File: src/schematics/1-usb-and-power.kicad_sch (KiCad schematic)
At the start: 0 parts

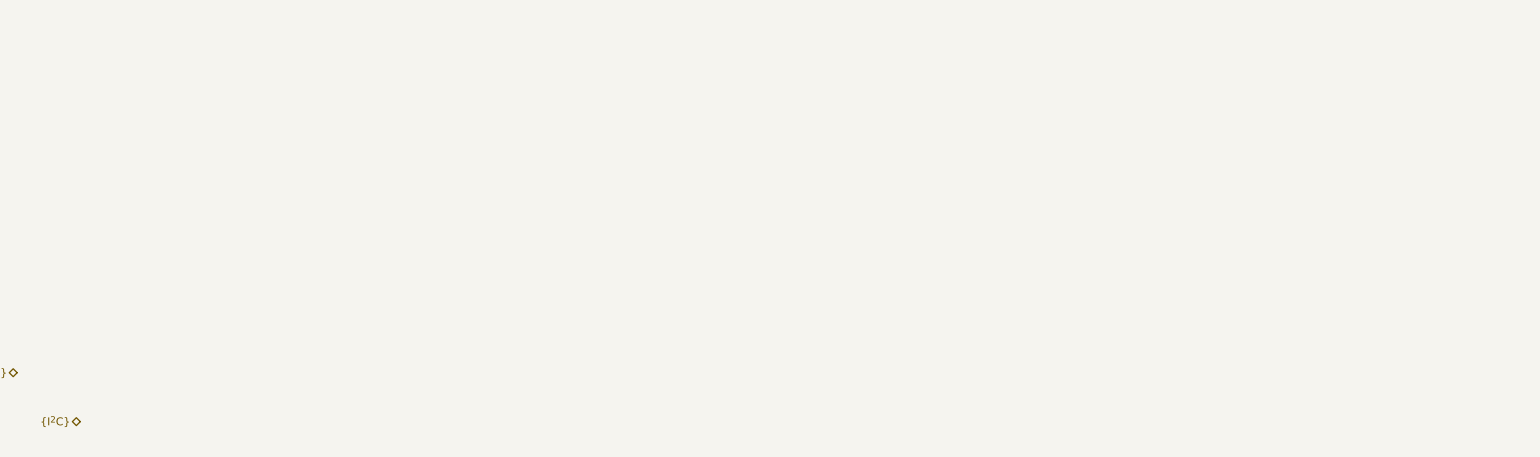
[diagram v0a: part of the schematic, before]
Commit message: Further MCU elaboration and pin mapping.
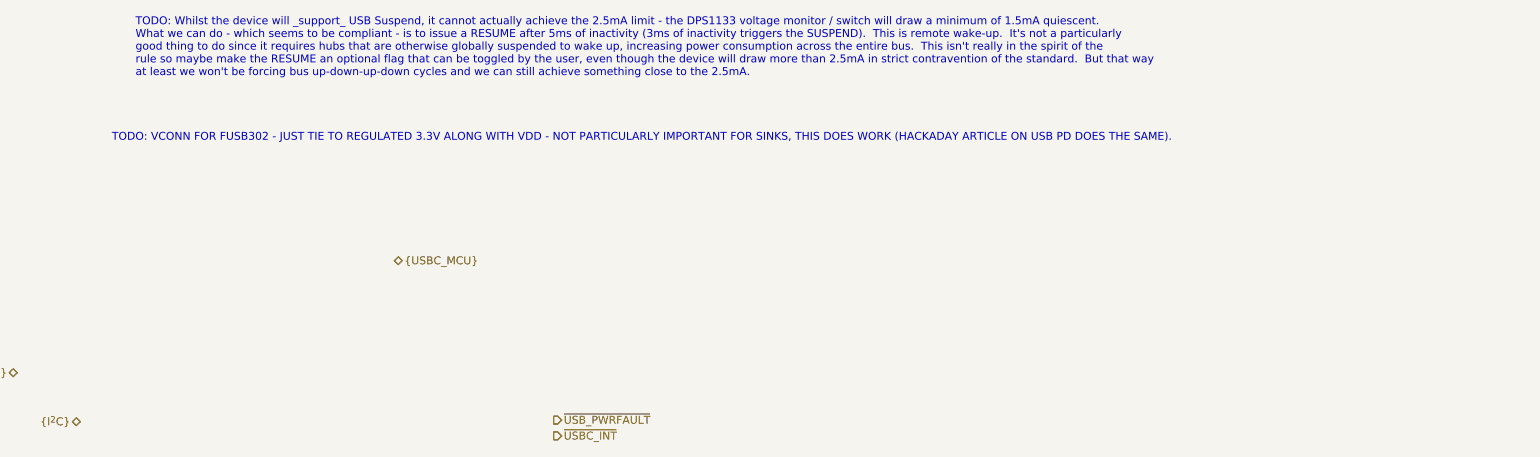
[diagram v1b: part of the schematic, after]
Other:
- note added: "TODO: VCONN FOR FUSB302 - JUST TIE TO REGULATED 3.3V ALONG WITH VDD - NOT PARTICULARLY IMPORTANT FOR SINKS, THIS DOES WORK (HACKADAY ARTICLE ON USB PD DOES THE SAME)."
- note added: "TODO: Whilst the device will _support_ USB Suspend, it cannot actually achieve the 2.5mA limit - the DPS1133 voltage monitor / switch will draw a minimum of 1.5mA quiescent. What we can do - which seems to be compliant - is to issue a RESUME after 5ms of inactivity (3ms of inactivity triggers the SUSPEND). This is remote wake-up. It's not a particularly good thing to do since it requires hubs tha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"
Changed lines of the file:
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@@
     (company "Pete Restall <pete@restall.net>")
+  )
+  (bus_alias "USBC_MCU" (members "D_{+}" "D_{-}"))
+  (text "TODO: VCONN FOR FUSB302 - JUST TIE TO REGULATED 3.3V ALONG WITH VDD - NOT PARTICULARLY IMPORTANT FOR SINKS, THIS DOES WORK (HACKADAY ARTICLE ON USB PD DOES THE SAME)."
+    (at 81.28 82.296 0)
+    (effects (font (size 1.27 1.27)) (justify left bottom))
+  )
+  (text "TODO: Whilst the device will _support_ USB Suspend, it cannot actually achieve the 2.5mA limit - the DPS1133 voltage monitor / switch will draw a minimum of 1.5mA quiescent.\nWhat we can do - which seems to be compliant - is to issue a RESUME after 5ms of inactivity (3ms of inactivity triggers the SUSPEND).  This is remote wake-up.  It's not a particularly\ngood thing to do since it requires hubs that are otherwise globally suspended to wake up, increasing power consumption across the entire bus.  This isn't really in the spirit of the\nrule so maybe make the RESUME an optional flag that can be toggled by the user, even though the device will draw more than 2.5mA in strict contravention of the standard.  But that way\nat least we won't be forcing bus up-down-up-down cycles and we can still achieve something close to the 2.5mA."
+    (at 85.09 71.882 0)
+    (effects (font (size 1.27 1.27)) (justify left bottom))
   )
   (hierarchical_label "{USBC_CONN}" (shape bidirectional) (at 66.04 119.38 180) (fields_autoplaced)
     (effects (font (size 1.27 1.27)) (justify right))
   )
+  (hierarchical_label "~{USBC_INT}" (shape output) (at 152.4 129.54 0) (fields_autoplaced)
+    (effects (font (size 1.27 1.27)) (justify left))
+  )
   (hierarchical_label "USBC_VBUS" (shape input) (at 50.8 101.346 180) (fields_autoplaced)
     (effects (font (size 1.27 1.27)) (justify right))
+  )
+  (hierarchical_label "{USBC_MCU}" (shape bidirectional) (at 126.746 101.346 0) (fields_autoplaced)
+    (effects (font (size 1.27 1.27)) (justify left))
   )
   (hierarchical_label "{I^{2}C}" (shape bidirectional) (at 76.2 127.254 180) (fields_autoplaced)
     (effects (font (size 1.27 1.27)) (justify right))
   )
+  (hierarchical_label "~{USB_PWRFAULT}" (shape output) (at 152.4 127 0) (fields_autoplaced)
+    (effects (font (size 1.27 1.27)) (justify left))
+  )
 )

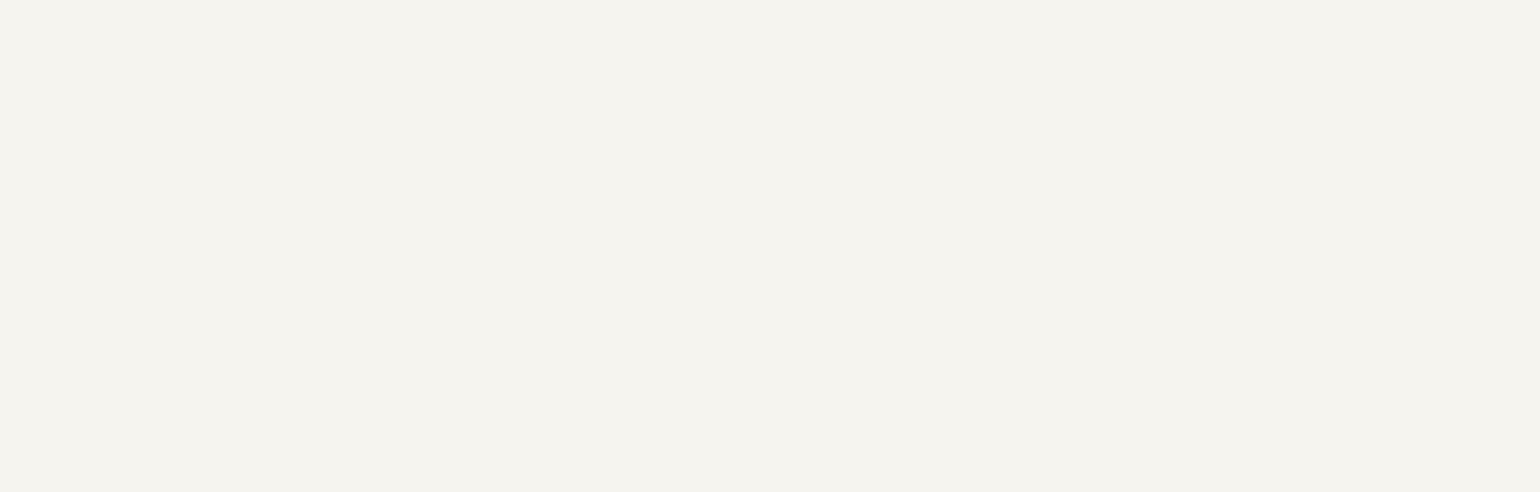
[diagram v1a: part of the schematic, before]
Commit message: Further elaboration of the design, particularly around the power budget.  It's clear that the USB Suspend current of 2.5mA won't be met, mainly due to the DPS1133 power switch's quiescent current.  This is a nice part worth keeping though as it contains OVP, OCP and reverse voltage protection all in one, up to 24V maximum input.
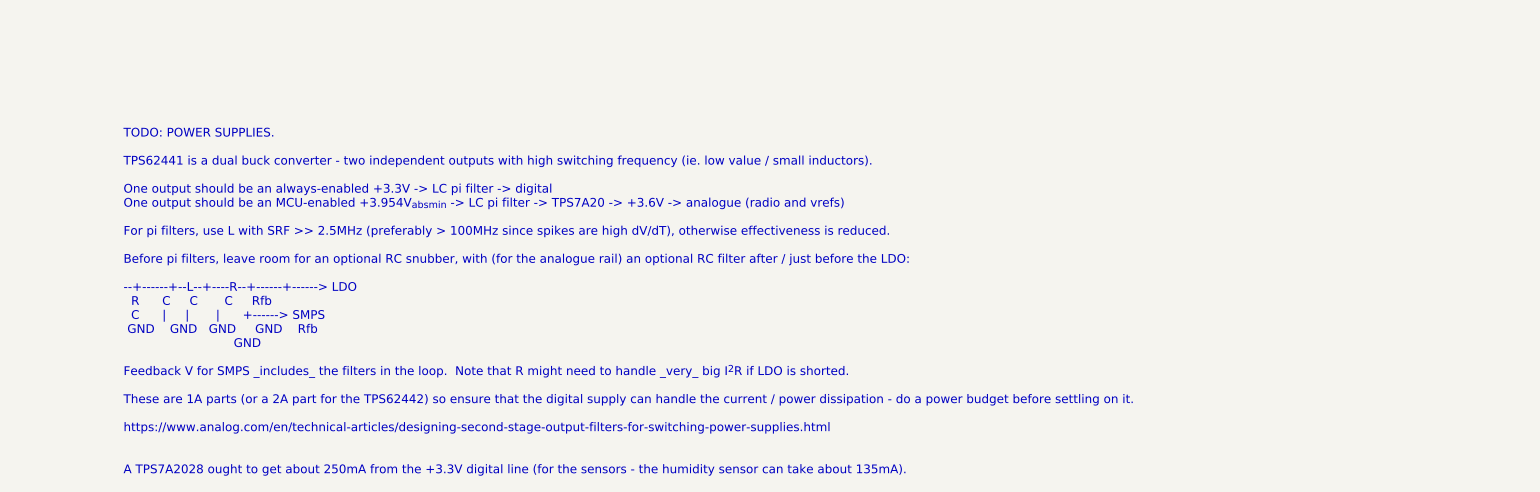
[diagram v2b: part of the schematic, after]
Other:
- note added: "TODO: POWER SUPPLIES. TPS62441 is a dual buck converter - two independent outputs with high switching frequency (ie. low value / small inductors). One output should be an always-enabled +3.3V -> LC pi filter -> digital One output should be an MCU-enabled +3.954V_{absmin} -> LC pi filter -> TPS7A20 -> +3.6V -> analogue (radio and vrefs) For pi filters, use L with SRF >> 2.5MHz (preferably > 100MHz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"
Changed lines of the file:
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@@
+    (effects (font (size 1.27 1.27)) (justify left bottom))
+  )
+  (text "TODO: POWER SUPPLIES.\n\nTPS62441 is a dual buck converter - two independent outputs with high switching frequency (ie. low value / small inductors).\n\nOne output should be an always-enabled +3.3V -> LC pi filter -> digital\nOne output should be an MCU-enabled +3.954V_{absmin} -> LC pi filter -> TPS7A20 -> +3.6V -> analogue (radio and vrefs)\n\nFor pi filters, use L with SRF >> 2.5MHz (preferably > 100MHz since spikes are high dV/dT), otherwise effectiveness is reduced.\n\nBefore pi filters, leave room for an optional RC snubber, with (for the analogue rail) an optional RC filter after / just before the LDO:\n\n--+------+--L--+----R--+------+------> LDO\n  R      C     C       C     Rfb\n  C      |     |       |      +------> SMPS\n GND    GND   GND     GND    Rfb\n                             GND\n\nFeedback V for SMPS _includes_ the filters in the loop.  Note that R might need to handle _very_ big I^{2}R if LDO is shorted.\n\nThese are 1A parts (or a 2A part for the TPS62442) so ensure that the digital supply can handle the current / power dissipation - do a power budget before settling on it.\n\nhttps://www.analog.com/en/technical-articles/designing-second-stage-output-filters-for-switching-power-supplies.html\n\n\nA TPS7A2028 ought to get about 250mA from the +3.3V digital line (for the sensors - the humidity sensor can take about 135mA).\n"
+    (at 138.176 209.804 0)
     (effects (font (size 1.27 1.27)) (justify left bottom))
   )

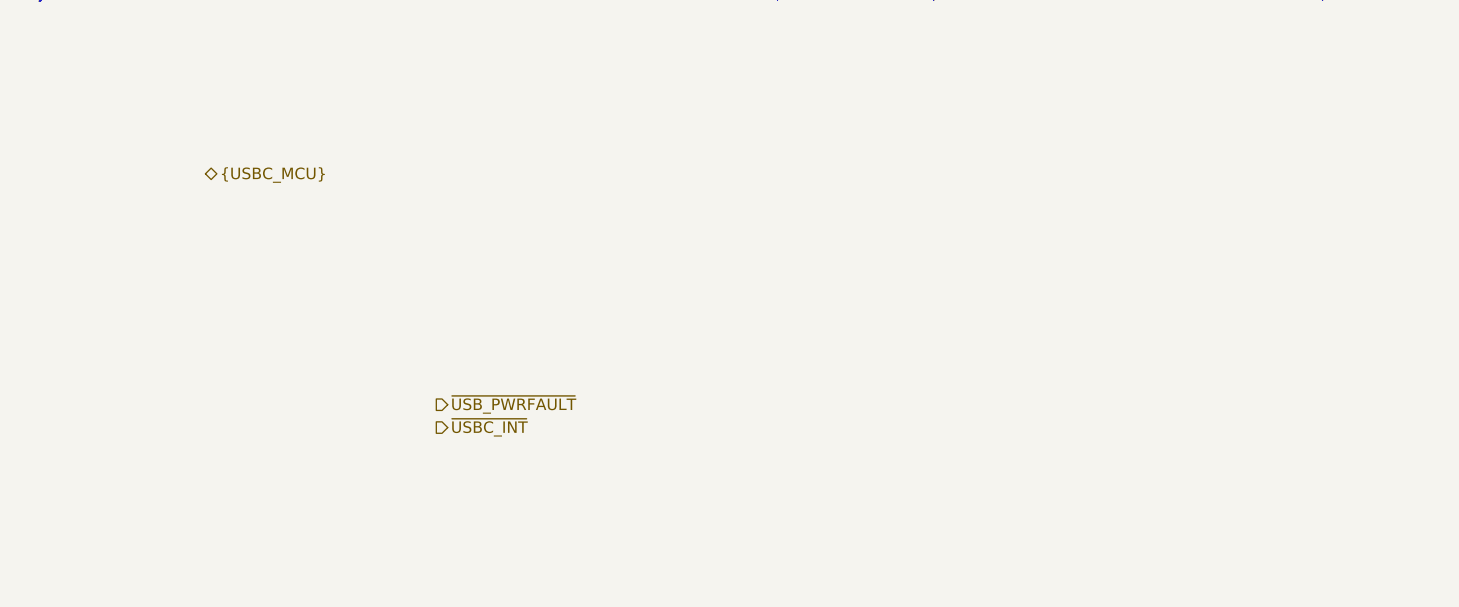
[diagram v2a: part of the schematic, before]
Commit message: Elaboration of the top-level schematicd.
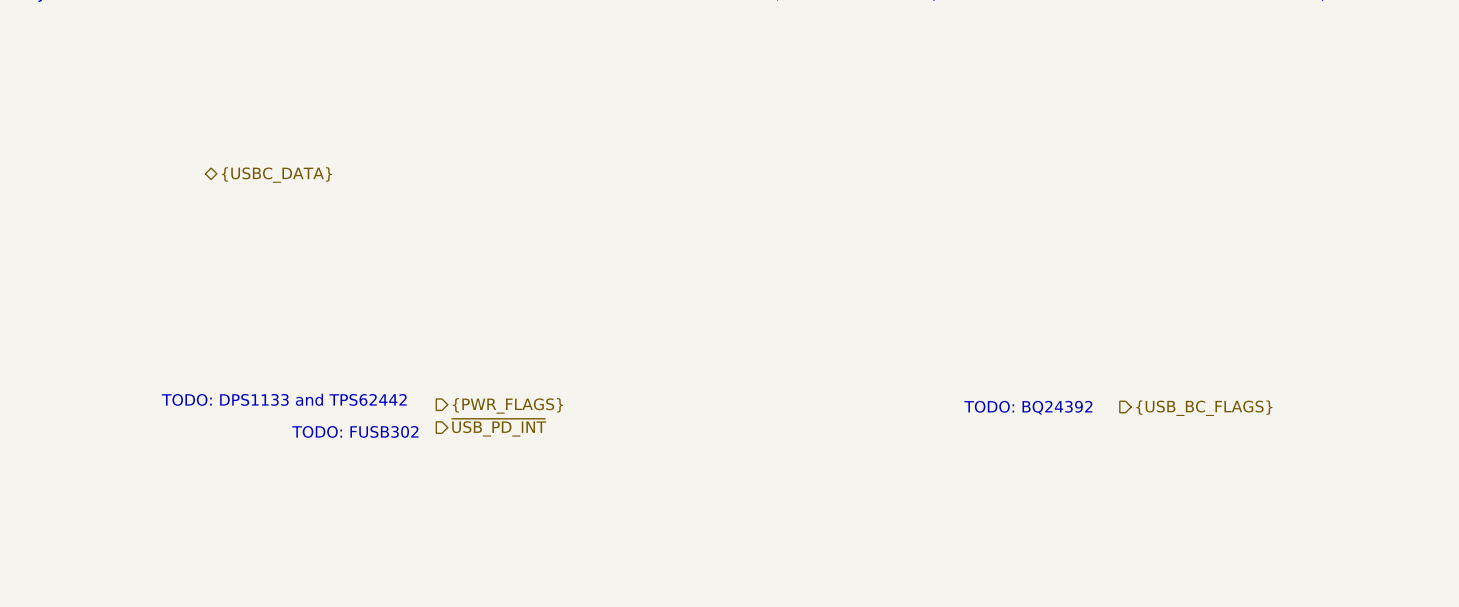
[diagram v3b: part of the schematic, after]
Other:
- note added: "TODO: BQ24392"
- note added: "TODO: DPS1133 and TPS62442"
- note added: "TODO: FUSB302"
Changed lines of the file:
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@@
     (company "Pete Restall <pete@restall.net>")
   )
-  (bus_alias "USBC_MCU" (members "D_{+}" "D_{-}"))
+  (bus_alias "PWR_FLAGS" (members "~{USBC_FAULT}" "~{MCU_REG_FAULT}" "~{MSF_REG_FAULT}"))
+  (bus_alias "USB_DATA" (members "D_{+}" "D_{-}"))
   (text "TODO: VCONN FOR FUSB302 - JUST TIE TO REGULATED 3.3V ALONG WITH VDD - NOT PARTICULARLY IMPORTANT FOR SINKS, THIS DOES WORK (HACKADAY ARTICLE ON USB PD DOES THE SAME)."
     (at 81.28 82.296 0)
     (effects (font (size 1.27 1.27)) (justify left bottom))
   )
+  (text "TODO: BQ24392" (at 211.074 128.27 0)
+    (effects (font (size 1.27 1.27)) (justify left bottom))
+  )
+  (text "TODO: DPS1133 and TPS62442" (at 121.92 127.508 0)
+    (effects (font (size 1.27 1.27)) (justify left bottom))
+  )
   (text "TODO: Whilst the device will _support_ USB Suspend, it cannot actually achieve the 2.5mA limit - the DPS1133 voltage monitor / switch will draw a minimum of 1.5mA quiescent.\nWhat we can do - which seems to be compliant - is to issue a RESUME after 5ms of inactivity (3ms of inactivity triggers the SUSPEND).  This is remote wake-up.  It's not a particularly\ngood thing to do since it requires hubs that are otherwise globally suspended to wake up, increasing power consumption across the entire bus.  This isn't really in the spirit of the\nrule so maybe make the RESUME an optional flag that can be toggled by the user, even though the device will draw more than 2.5mA in strict contravention of the standard.  But that way\nat least we won't be forcing bus up-down-up-down cycles and we can still achieve something close to the 2.5mA."
     (at 85.09 71.882 0)
+    (effects (font (size 1.27 1.27)) (justify left bottom))
+  )
+  (text "TODO: FUSB302" (at 136.398 131.064 0)
     (effects (font (size 1.27 1.27)) (justify left bottom))
   )
@@
     (effects (font (size 1.27 1.27)) (justify right))
   )
-  (hierarchical_label "~{USBC_INT}" (shape output) (at 152.4 129.54 0) (fields_autoplaced)
+  (hierarchical_label "~{USB_PD_INT}" (shape output) (at 152.4 129.54 0) (fields_autoplaced)
     (effects (font (size 1.27 1.27)) (justify left))
   )
@@
     (effects (font (size 1.27 1.27)) (justify right))
   )
-  (hierarchical_label "{USBC_MCU}" (shape bidirectional) (at 126.746 101.346 0) (fields_autoplaced)
+  (hierarchical_label "{USBC_DATA}" (shape bidirectional) (at 126.746 101.346 0) (fields_autoplaced)
     (effects (font (size 1.27 1.27)) (justify left))
   )
@@
     (effects (font (size 1.27 1.27)) (justify right))
   )
-  (hierarchical_label "~{USB_PWRFAULT}" (shape output) (at 152.4 127 0) (fields_autoplaced)
+  (hierarchical_label "{PWR_FLAGS}" (shape output) (at 152.4 127 0) (fields_autoplaced)
     (effects (font (size 1.27 1.27)) (justify left))
   )
+  (hierarchical_label "{USB_BC_FLAGS}" (shape output) (at 228.346 127.254 0) (fields_autoplaced)
+    (effects (font (size 1.27 1.27)) (justify left))
+  )
